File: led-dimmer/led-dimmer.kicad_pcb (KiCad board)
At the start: 2 copper layers, 27.6 x 30.5 mm, 24 parts, among them J1 Conn_01x02_Pin, J2 Conn_01x02_Pin, Q1 IRLML6344, U1 NE555P

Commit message: Updated LED Dimmer PCB decoupling capacitor placement on pin 8
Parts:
- R3: value H50115K1A -> RK09711100F8
- moved C4 12.5 mm to (91.2, 116.1), turned to 90 degrees
- moved R1 2.98 mm to (90.8, 119.4)
- moved D1 0.38 mm to (88.9, 120.3)
- moved D2 0.27 mm to (81.2, 120.3)
- moved G*** 0.22 mm to (95.6, 120.3)
- moved G*** 0.22 mm to (95.6, 123.6)
- moved G*** 0.08 mm to (74.4, 123.6)
- moved G*** 0.08 mm to (74.4, 120.3)
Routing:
- net +12V: track 35.4 -> 37.4 mm
- net DISCHARGE: track 12.3 -> 11.7 mm
- net GND: vias 44 -> 26
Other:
- board text added: "LED Dimmer Rev. 1.4"
- board text removed: "LED Dimmer Rev. 1.3"

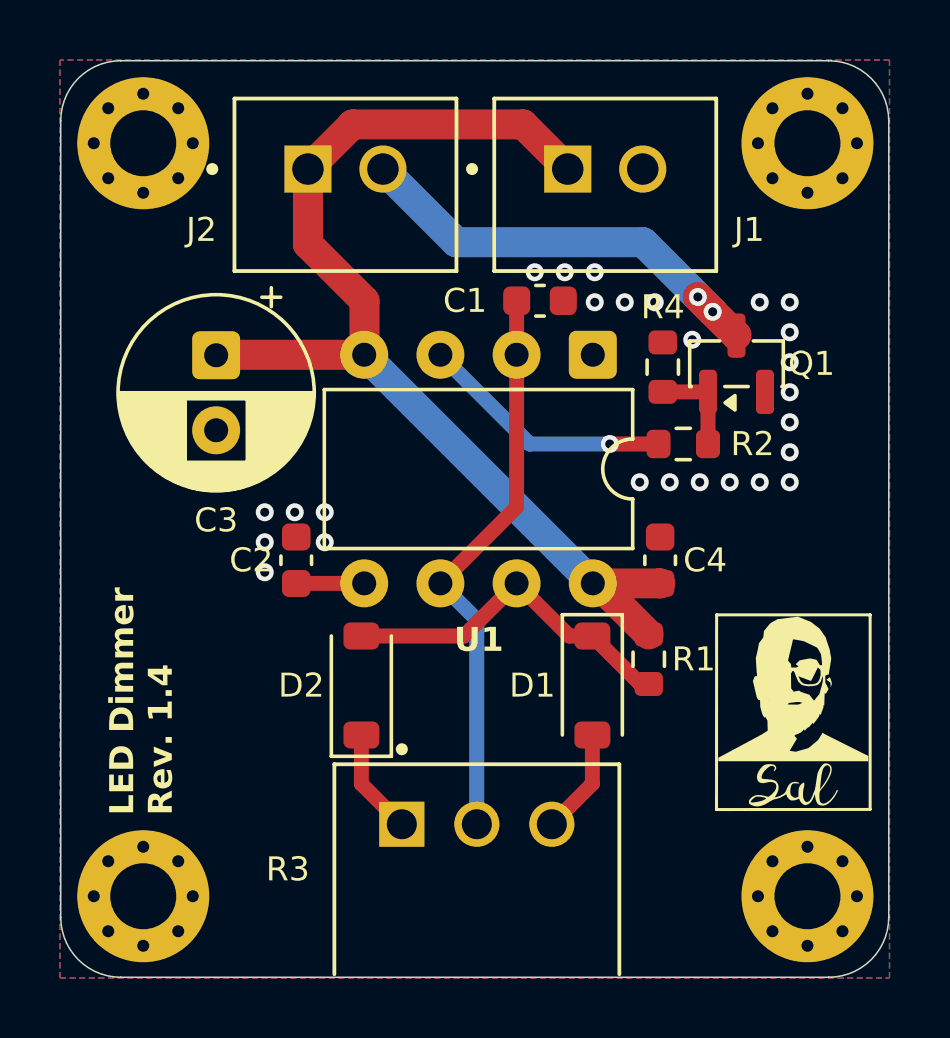
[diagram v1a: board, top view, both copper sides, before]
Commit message: LED Dimmer - reorganized project libraries into libs directory
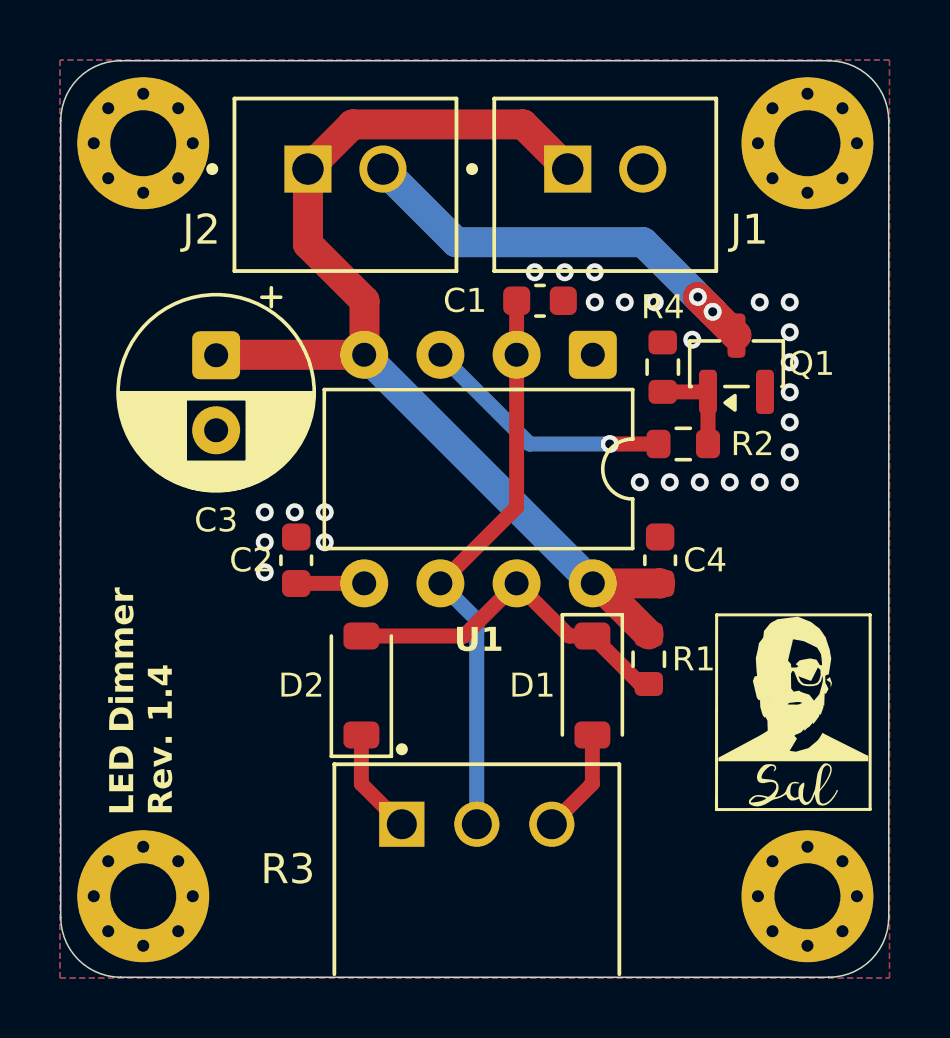
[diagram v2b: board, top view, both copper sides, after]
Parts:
- removed the G*** at (95.6, 120.3)
- removed the G*** at (95.6, 123.6)
- removed the G*** at (74.4, 123.6)
- removed the G*** at (74.4, 120.3)
- added G***: LOGO, sal_footprints:SalLogo, F.Cu at (95.6, 120.3)
- added G***: LOGO, sal_footprints:SalSig, F.Cu at (95.6, 123.6)
- added G***: LOGO, sal_footprints:SalLogo, B.Cu at (74.4, 120.3)
- added G***: LOGO, sal_footprints:SalSig, B.Cu at (74.4, 123.6)
- J1, J2: footprint footprints:JST_B2B-XH-A -> external_footprints:JST_B2B-XH-A
- R3: footprint footprints:TRIM_PTN091-H50115K1A -> external_footprints:TRIM_PTN091-H50115K1A

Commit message: LED Dimmer - Re-introduce ground vias
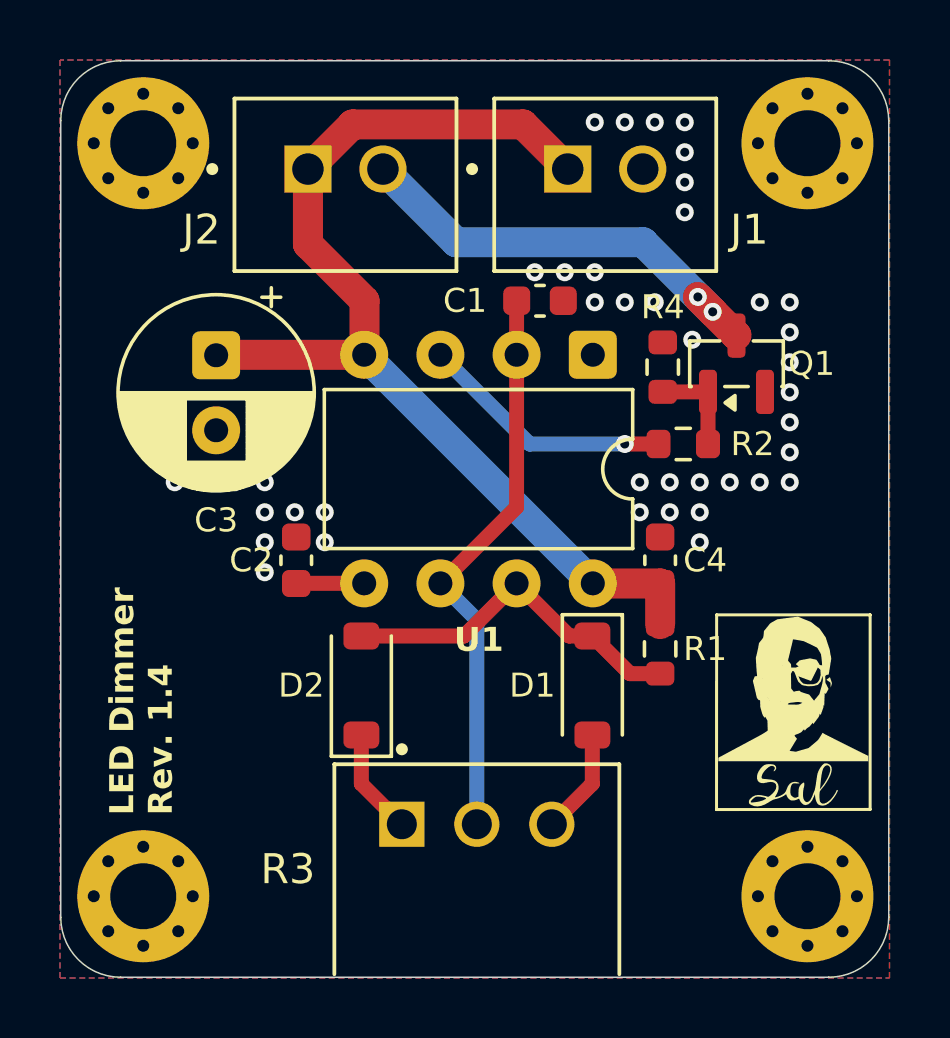
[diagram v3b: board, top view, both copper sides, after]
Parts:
- moved R1 0.51 mm to (91.2, 119.1)
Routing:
- net +12V: track 37.4 -> 36.6 mm
- net GND: vias 26 -> 45
